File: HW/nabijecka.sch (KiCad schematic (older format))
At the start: 10 parts

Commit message: add some codes for JLCPCB, change package and schematic of CP2102
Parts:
- C? (x2): footprint Capacitor_SMD:C_1206_3216Metric -> Capacitor_SMD:C_0402_1005Metric; LCSC (none) -> C15525
- R? (x2): LCSC (none) -> C11702
- R?: LCSC (none) -> C25086
- U?: LCSC (none) -> C16581
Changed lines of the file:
@@
 F 2 "" H 4050 3750 50  0001 C CNN
 F 3 "" H 4050 3750 50  0001 C CNN
+F 4 "C16581" H 4500 3300 50  0001 C CNN "LCSC"
 	1    4500 3300
 	1    0    0    -1
@@
 F 2 "Resistor_SMD:R_0402_1005Metric" V 4730 2650 50  0001 C CNN
 F 3 "~" H 4800 2650 50  0001 C CNN
+F 4 "C11702" H 4800 2650 50  0001 C CNN "LCSC"
 	1    4800 2650
 	0    1    1    0
@@
 F 0 "C?" H 5365 3796 50  0000 L CNN
 F 1 "10u" H 5365 3705 50  0000 L CNN
-F 2 "Capacitor_SMD:C_1206_3216Metric" H 5288 3600 50  0001 C CNN
+F 2 "Capacitor_SMD:C_0402_1005Metric" H 5288 3600 50  0001 C CNN
 F 3 "~" H 5250 3750 50  0001 C CNN
+F 4 "C15525" H 5250 3750 50  0001 C CNN "LCSC"
 	1    5250 3750
 	1    0    0    -1
@@
 F 2 "Resistor_SMD:R_0402_1005Metric" V 4080 2450 50  0001 C CNN
 F 3 "~" H 4150 2450 50  0001 C CNN
+F 4 "C25086" H 4150 2450 50  0001 C CNN "LCSC"
 	1    4150 2450
 	0    1    1    0
@@
 F 0 "C?" V 3298 2450 50  0000 C CNN
 F 1 "10u" V 3389 2450 50  0000 C CNN
-F 2 "Capacitor_SMD:C_1206_3216Metric" H 3588 2300 50  0001 C CNN
+F 2 "Capacitor_SMD:C_0402_1005Metric" H 3588 2300 50  0001 C CNN
 F 3 "~" H 3550 2450 50  0001 C CNN
+F 4 "C15525" H 3550 2450 50  0001 C CNN "LCSC"
 	1    3550 2450
 	0    1    1    0
@@
 F 2 "Resistor_SMD:R_0402_1005Metric" V 4730 2300 50  0001 C CNN
 F 3 "~" H 4800 2300 50  0001 C CNN
+F 4 "C11702" H 4800 2300 50  0001 C CNN "LCSC"
 	1    4800 2300
 	0    1    1    0

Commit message: add some codes for JLCPCB
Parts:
- D?: LCSC (none) -> C2286
- D?: LCSC (none) -> C72043
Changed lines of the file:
@@
 F 2 "LED_SMD:LED_0603_1608Metric" H 5300 2300 50  0001 C CNN
 F 3 "~" H 5300 2300 50  0001 C CNN
+F 4 "C72043" H 5300 2300 50  0001 C CNN "LCSC"
 	1    5300 2300
 	-1   0    0    1
@@
 F 2 "LED_SMD:LED_0603_1608Metric" H 5300 2650 50  0001 C CNN
 F 3 "~" H 5300 2650 50  0001 C CNN
+F 4 "C2286" H 5300 2650 50  0001 C CNN "LCSC"
 	1    5300 2650
 	-1   0    0    1

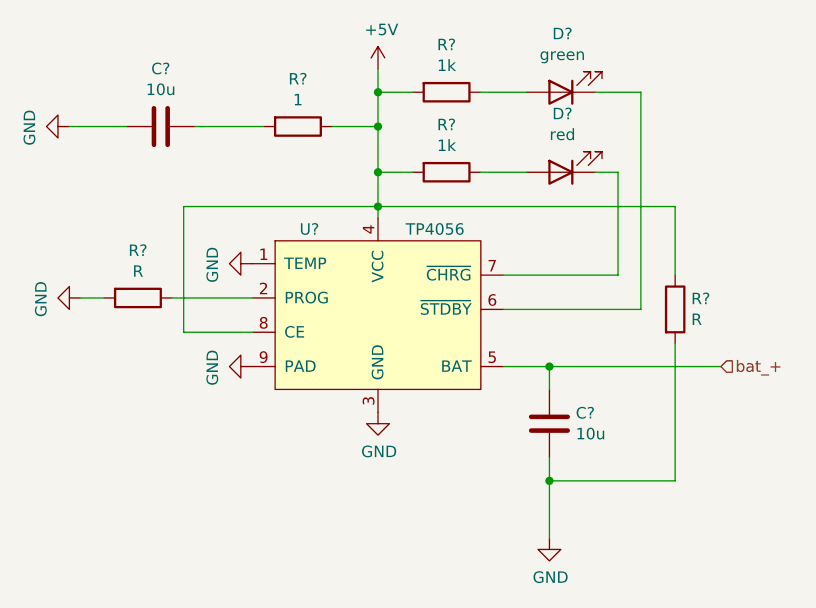
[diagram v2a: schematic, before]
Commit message: add footprint of inductor, add codes for JLCPCB, repair mistakes
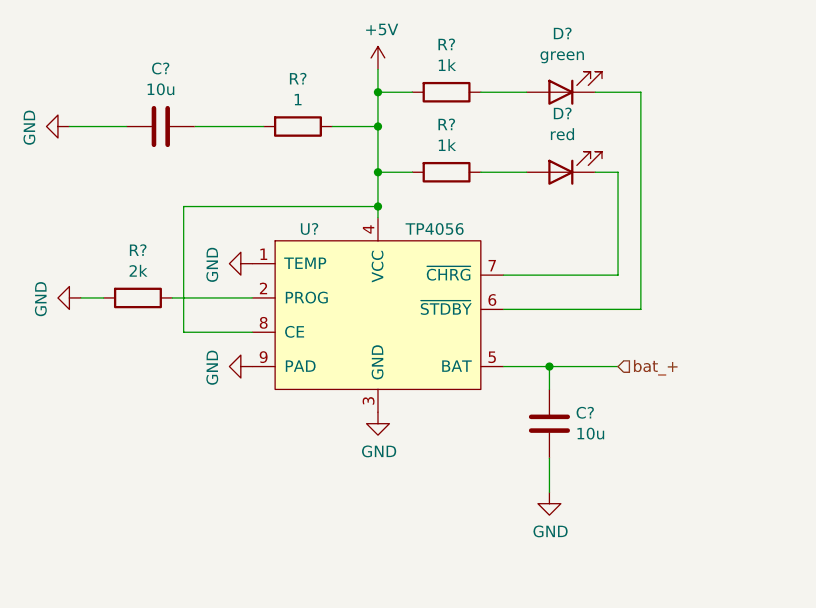
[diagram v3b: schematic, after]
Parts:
- removed R?: R, Resistor_SMD:R_0402_1005Metric, symbol Device:R
- R?: value R -> 2k; LCSC (none) -> C4109
- U?: footprint (none) -> Package_SO:SOP-8_3.9x4.9mm_P1.27mm
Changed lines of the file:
@@
 F 0 "U?" H 4200 3700 50  0000 C CNN
 F 1 "TP4056" H 4750 3700 50  0000 C CNN
-F 2 "" H 4050 3750 50  0001 C CNN
+F 2 "Package_SO:SOP-8_3.9x4.9mm_P1.27mm" H 4050 3750 50  0001 C CNN
 F 3 "" H 4050 3750 50  0001 C CNN
 F 4 "C16581" H 4500 3300 50  0001 C CNN "LCSC"
@@
 P 3450 3200
 F 0 "R?" V 3243 3200 50  0000 C CNN
-F 1 "R" V 3334 3200 50  0000 C CNN
+F 1 "2k" V 3334 3200 50  0000 C CNN
 F 2 "Resistor_SMD:R_0402_1005Metric" V 3380 3200 50  0001 C CNN
 F 3 "~" H 3450 3200 50  0001 C CNN
+F 4 "C4109" H 3450 3200 50  0001 C CNN "LCSC"
 	1    3450 3200
 	0    1    1    0
@@
 	4500 2450 4500 2300
 $Comp
-L power:GND #PWR?
-U 1 1 5F728484
-P 5250 4250
-F 0 "#PWR?" H 5250 4000 50  0001 C CNN
-F 1 "GND" H 5255 4077 50  0000 C CNN
-F 2 "" H 5250 4250 50  0001 C CNN
-F 3 "" H 5250 4250 50  0001 C CNN
-	1    5250 4250
-	1    0    0    -1
-$EndComp
-$Comp
 L Device:C C?
 U 1 1 5F728700
@@
 Wire Wire Line
 	5250 3500 5050 3500
-$Comp
-L Device:R R?
-U 1 1 5F72B67D
-P 5800 3250
-F 0 "R?" H 5870 3296 50  0000 L CNN
-F 1 "R" H 5870 3205 50  0000 L CNN
-F 2 "Resistor_SMD:R_0402_1005Metric" V 5730 3250 50  0001 C CNN
-F 3 "~" H 5800 3250 50  0001 C CNN
-	1    5800 3250
-	1    0    0    -1
-$EndComp
-Wire Wire Line
-	5800 3100 5800 2800
-Wire Wire Line
-	5800 2800 4500 2800
-Wire Wire Line
-	5250 3500 6000 3500
+Wire Wire Line
+	5250 3500 5550 3500
 Connection ~ 5250 3500
-Text HLabel 6000 3500 2    50   Input ~ 0
-bat_+
 $Comp
 L Device:R R?
@@
 Wire Wire Line
 	3400 2450 3150 2450
-Wire Wire Line
-	5800 3400 5800 4000
 $Comp
 L Device:LED D?
@@
 Wire Wire Line
 	4500 2650 4500 2450
-Wire Wire Line
-	5250 3900 5250 4000
-Wire Wire Line
-	5800 4000 5250 4000
-Connection ~ 5250 4000
-Wire Wire Line
-	5250 4000 5250 4250
 $Comp
 L power:GND #PWR?
@@
 	0    1    1    0
 $EndComp
+Text HLabel 5550 3500 2    50   Input ~ 0
+bat_+
+Wire Wire Line
+	5250 3900 5250 4050
+$Comp
+L power:GND #PWR?
+U 1 1 5F728484
+P 5250 4050
+F 0 "#PWR?" H 5250 3800 50  0001 C CNN
+F 1 "GND" H 5255 3877 50  0000 C CNN
+F 2 "" H 5250 4050 50  0001 C CNN
+F 3 "" H 5250 4050 50  0001 C CNN
+	1    5250 4050
+	1    0    0    -1
+$EndComp
 $EndSCHEMATC

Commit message: numbering components, place components on board
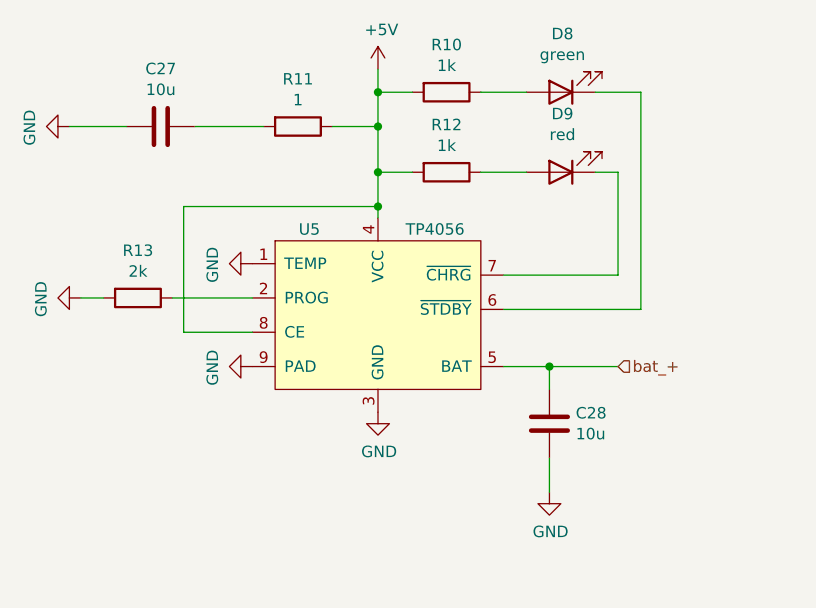
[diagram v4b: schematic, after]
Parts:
- U5: renamed from U?; footprint Package_SO:SOP-8_3.9x4.9mm_P1.27mm -> Package_SO:SOP-8-1EP_4.57x4.57mm_P1.27mm_EP4.57x4.45mm
- gave numbers to parts that had none: 8
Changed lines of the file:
@@
 $EndDescr
 $Comp
-L power:+5V #PWR?
+L power:+5V #PWR0141
 U 1 1 5F75411E
 P 4500 2200
-F 0 "#PWR?" H 4500 2050 50  0001 C CNN
+F 0 "#PWR0141" H 4500 2050 50  0001 C CNN
 F 1 "+5V" H 4515 2373 50  0000 C CNN
 F 2 "" H 4500 2200 50  0001 C CNN
@@
 $EndComp
 $Comp
-L symbols:TP4056 U?
+L symbols:TP4056 U5
 U 1 1 5F720A93
 P 4500 3300
-F 0 "U?" H 4200 3700 50  0000 C CNN
+F 0 "U5" H 4200 3700 50  0000 C CNN
 F 1 "TP4056" H 4750 3700 50  0000 C CNN
-F 2 "Package_SO:SOP-8_3.9x4.9mm_P1.27mm" H 4050 3750 50  0001 C CNN
+F 2 "Package_SO:SOP-8-1EP_4.57x4.57mm_P1.27mm_EP4.57x4.45mm" H 4050 3750 50  0001 C CNN
 F 3 "" H 4050 3750 50  0001 C CNN
 F 4 "C16581" H 4500 3300 50  0001 C CNN "LCSC"
@@
 	4500 2850 4500 2800
 $Comp
-L power:GND #PWR?
+L power:GND #PWR0142
 U 1 1 5F721445
 P 4500 3700
-F 0 "#PWR?" H 4500 3450 50  0001 C CNN
+F 0 "#PWR0142" H 4500 3450 50  0001 C CNN
 F 1 "GND" H 4505 3527 50  0000 C CNN
 F 2 "" H 4500 3700 50  0001 C CNN
@@
 	4500 2800 4500 2650
 $Comp
-L Device:R R?
+L Device:R R13
 U 1 1 5F721EB5
 P 3450 3200
-F 0 "R?" V 3243 3200 50  0000 C CNN
+F 0 "R13" V 3243 3200 50  0000 C CNN
 F 1 "2k" V 3334 3200 50  0000 C CNN
 F 2 "Resistor_SMD:R_0402_1005Metric" V 3380 3200 50  0001 C CNN
@@
 	3600 3200 3950 3200
 $Comp
-L power:GND #PWR?
+L power:GND #PWR0143
 U 1 1 5F724768
 P 3200 3200
-F 0 "#PWR?" H 3200 2950 50  0001 C CNN
+F 0 "#PWR0143" H 3200 2950 50  0001 C CNN
 F 1 "GND" H 3205 3027 50  0000 C CNN
 F 2 "" H 3200 3200 50  0001 C CNN
@@
 	3200 3200 3300 3200
 $Comp
-L power:GND #PWR?
+L power:GND #PWR0144
 U 1 1 5F724D56
 P 3950 3500
-F 0 "#PWR?" H 3950 3250 50  0001 C CNN
+F 0 "#PWR0144" H 3950 3250 50  0001 C CNN
 F 1 "GND" H 3955 3327 50  0000 C CNN
 F 2 "" H 3950 3500 50  0001 C CNN
@@
 $EndComp
 $Comp
-L Device:LED D?
+L Device:LED D8
 U 1 1 5F7276AF
 P 5300 2300
-F 0 "D?" H 5293 2045 50  0000 C CNN
+F 0 "D8" H 5293 2045 50  0000 C CNN
 F 1 "green" H 5293 2136 50  0000 C CNN
 F 2 "LED_SMD:LED_0603_1608Metric" H 5300 2300 50  0001 C CNN
@@
 $EndComp
 $Comp
-L Device:R R?
+L Device:R R12
 U 1 1 5F727AA2
 P 4800 2650
-F 0 "R?" V 4593 2650 50  0000 C CNN
+F 0 "R12" V 4593 2650 50  0000 C CNN
 F 1 "1k" V 4684 2650 50  0000 C CNN
 F 2 "Resistor_SMD:R_0402_1005Metric" V 4730 2650 50  0001 C CNN
@@
 	4500 2450 4500 2300
 $Comp
-L Device:C C?
+L Device:C C28
 U 1 1 5F728700
 P 5250 3750
-F 0 "C?" H 5365 3796 50  0000 L CNN
+F 0 "C28" H 5365 3796 50  0000 L CNN
 F 1 "10u" H 5365 3705 50  0000 L CNN
 F 2 "Capacitor_SMD:C_0402_1005Metric" H 5288 3600 50  0001 C CNN
@@
 Connection ~ 5250 3500
 $Comp
-L Device:R R?
+L Device:R R11
 U 1 1 5F72F879
 P 4150 2450
-F 0 "R?" V 3943 2450 50  0000 C CNN
+F 0 "R11" V 3943 2450 50  0000 C CNN
 F 1 "1" V 4034 2450 50  0000 C CNN
 F 2 "Resistor_SMD:R_0402_1005Metric" V 4080 2450 50  0001 C CNN
@@
 $EndComp
 $Comp
-L Device:C C?
+L Device:C C27
 U 1 1 5F72FAB8
 P 3550 2450
-F 0 "C?" V 3298 2450 50  0000 C CNN
+F 0 "C27" V 3298 2450 50  0000 C CNN
 F 1 "10u" V 3389 2450 50  0000 C CNN
 F 2 "Capacitor_SMD:C_0402_1005Metric" H 3588 2300 50  0001 C CNN
@@
 	4000 2450 3700 2450
 $Comp
-L power:GND #PWR?
+L power:GND #PWR0145
 U 1 1 5F730B44
 P 3150 2450
-F 0 "#PWR?" H 3150 2200 50  0001 C CNN
+F 0 "#PWR0145" H 3150 2200 50  0001 C CNN
 F 1 "GND" H 3155 2277 50  0000 C CNN
 F 2 "" H 3150 2450 50  0001 C CNN
@@
 	3400 2450 3150 2450
 $Comp
-L Device:LED D?
+L Device:LED D9
 U 1 1 5F726EA3
 P 5300 2650
-F 0 "D?" H 5293 2395 50  0000 C CNN
+F 0 "D9" H 5293 2395 50  0000 C CNN
 F 1 "red" H 5293 2486 50  0000 C CNN
 F 2 "LED_SMD:LED_0603_1608Metric" H 5300 2650 50  0001 C CNN
@@
 	5650 2300 5450 2300
 $Comp
-L Device:R R?
+L Device:R R10
 U 1 1 5F7352CE
 P 4800 2300
-F 0 "R?" V 4593 2300 50  0000 C CNN
+F 0 "R10" V 4593 2300 50  0000 C CNN
 F 1 "1k" V 4684 2300 50  0000 C CNN
 F 2 "Resistor_SMD:R_0402_1005Metric" V 4730 2300 50  0001 C CNN
@@
 	4500 2650 4500 2450
 $Comp
-L power:GND #PWR?
+L power:GND #PWR0146
 U 1 1 5F73C370
 P 3950 3050
-F 0 "#PWR?" H 3950 2800 50  0001 C CNN
+F 0 "#PWR0146" H 3950 2800 50  0001 C CNN
 F 1 "GND" H 3955 2877 50  0000 C CNN
 F 2 "" H 3950 3050 50  0001 C CNN
@@
 	5250 3900 5250 4050
 $Comp
-L power:GND #PWR?
+L power:GND #PWR0147
 U 1 1 5F728484
 P 5250 4050
-F 0 "#PWR?" H 5250 3800 50  0001 C CNN
+F 0 "#PWR0147" H 5250 3800 50  0001 C CNN
 F 1 "GND" H 5255 3877 50  0000 C CNN
 F 2 "" H 5250 4050 50  0001 C CNN

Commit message: repair package of TP4056
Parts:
- U5: footprint Package_SO:SOP-8-1EP_4.57x4.57mm_P1.27mm_EP4.57x4.45mm -> my_library:TP4056
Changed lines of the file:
@@
 F 0 "U5" H 4200 3700 50  0000 C CNN
 F 1 "TP4056" H 4750 3700 50  0000 C CNN
-F 2 "Package_SO:SOP-8-1EP_4.57x4.57mm_P1.27mm_EP4.57x4.45mm" H 4050 3750 50  0001 C CNN
+F 2 "my_library:TP4056" H 4050 3750 50  0001 C CNN
 F 3 "" H 4050 3750 50  0001 C CNN
 F 4 "C16581" H 4500 3300 50  0001 C CNN "LCSC"

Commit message: ready for first prototype
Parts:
- U5: JLCPCB_CORRECTION (none) -> 0;0;270
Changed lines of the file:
@@
 F 3 "" H 4050 3750 50  0001 C CNN
 F 4 "C16581" H 4500 3300 50  0001 C CNN "LCSC"
+F 5 "0;0;270" H 4500 3300 50  0001 C CNN "JLCPCB_CORRECTION"
 	1    4500 3300
 	1    0    0    -1
